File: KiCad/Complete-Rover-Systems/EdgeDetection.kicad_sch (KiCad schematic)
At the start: 9 parts, among them U1 ITR8307-F43, U10 74LS151, U3 ITR8307-F43, U4 ITR8307-F43, U5 ITR8307-F43, U6 ITR8307-F43, U7 ITR8307-F43, U8 ITR8307-F43, U9 ITR8307-F43

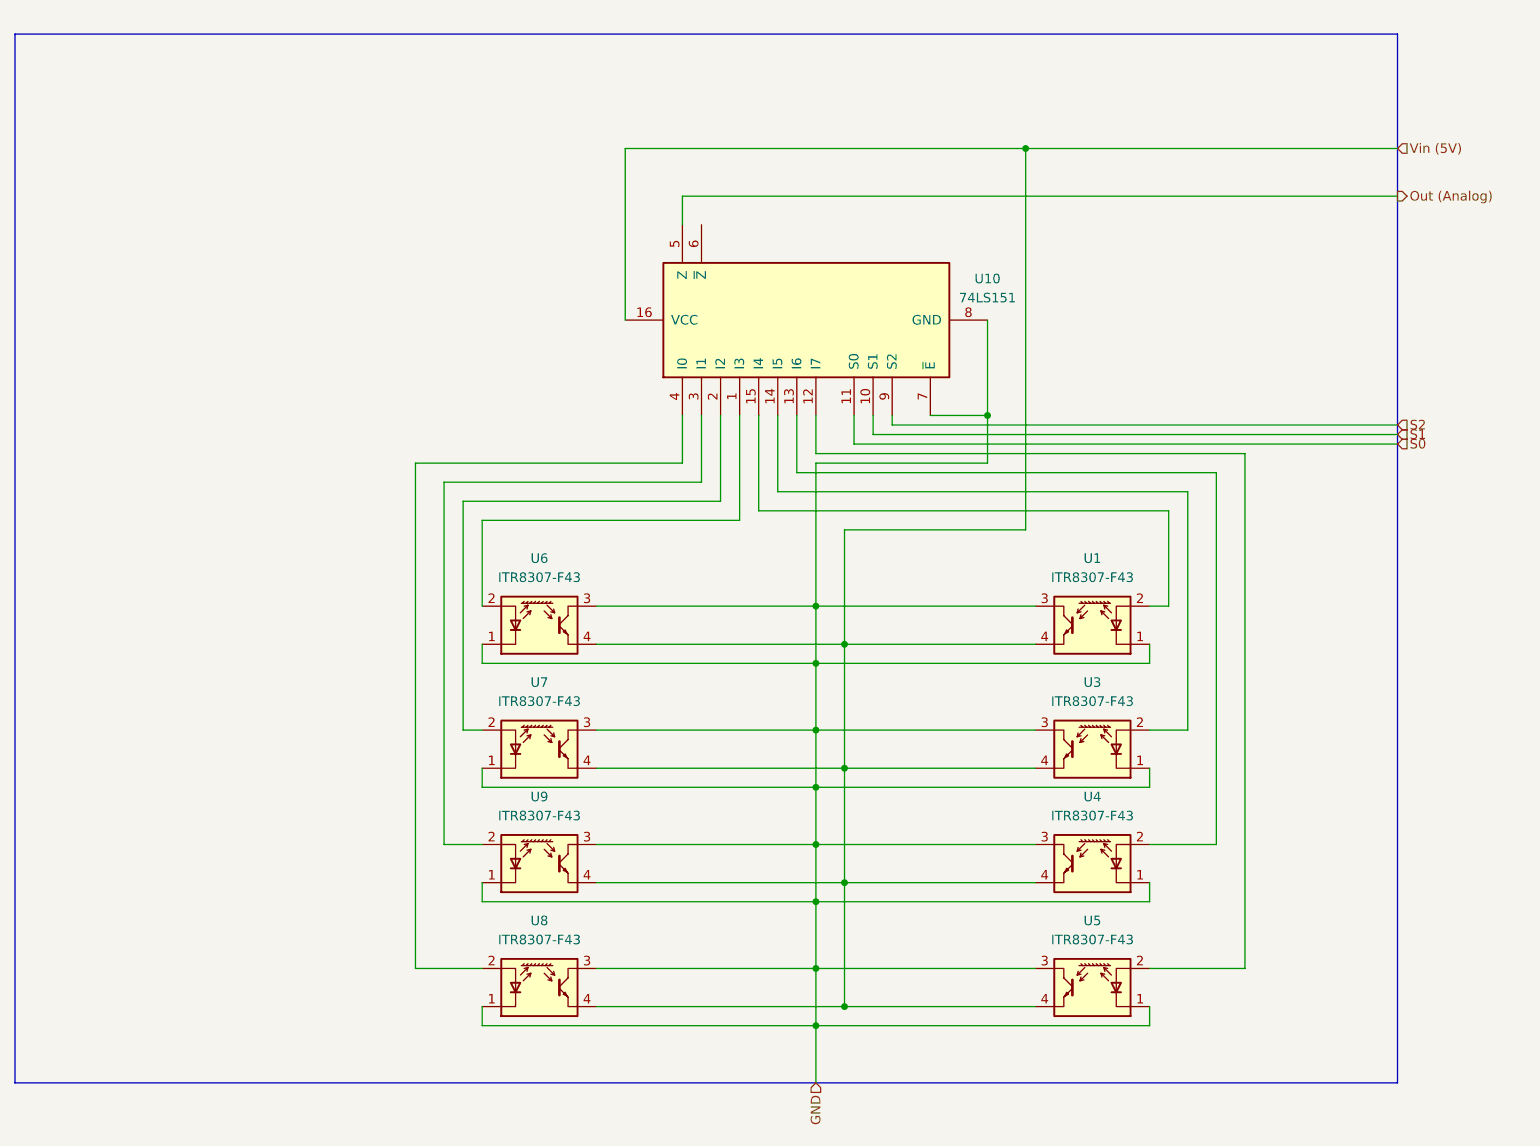
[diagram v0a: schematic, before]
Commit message: edge detection fix
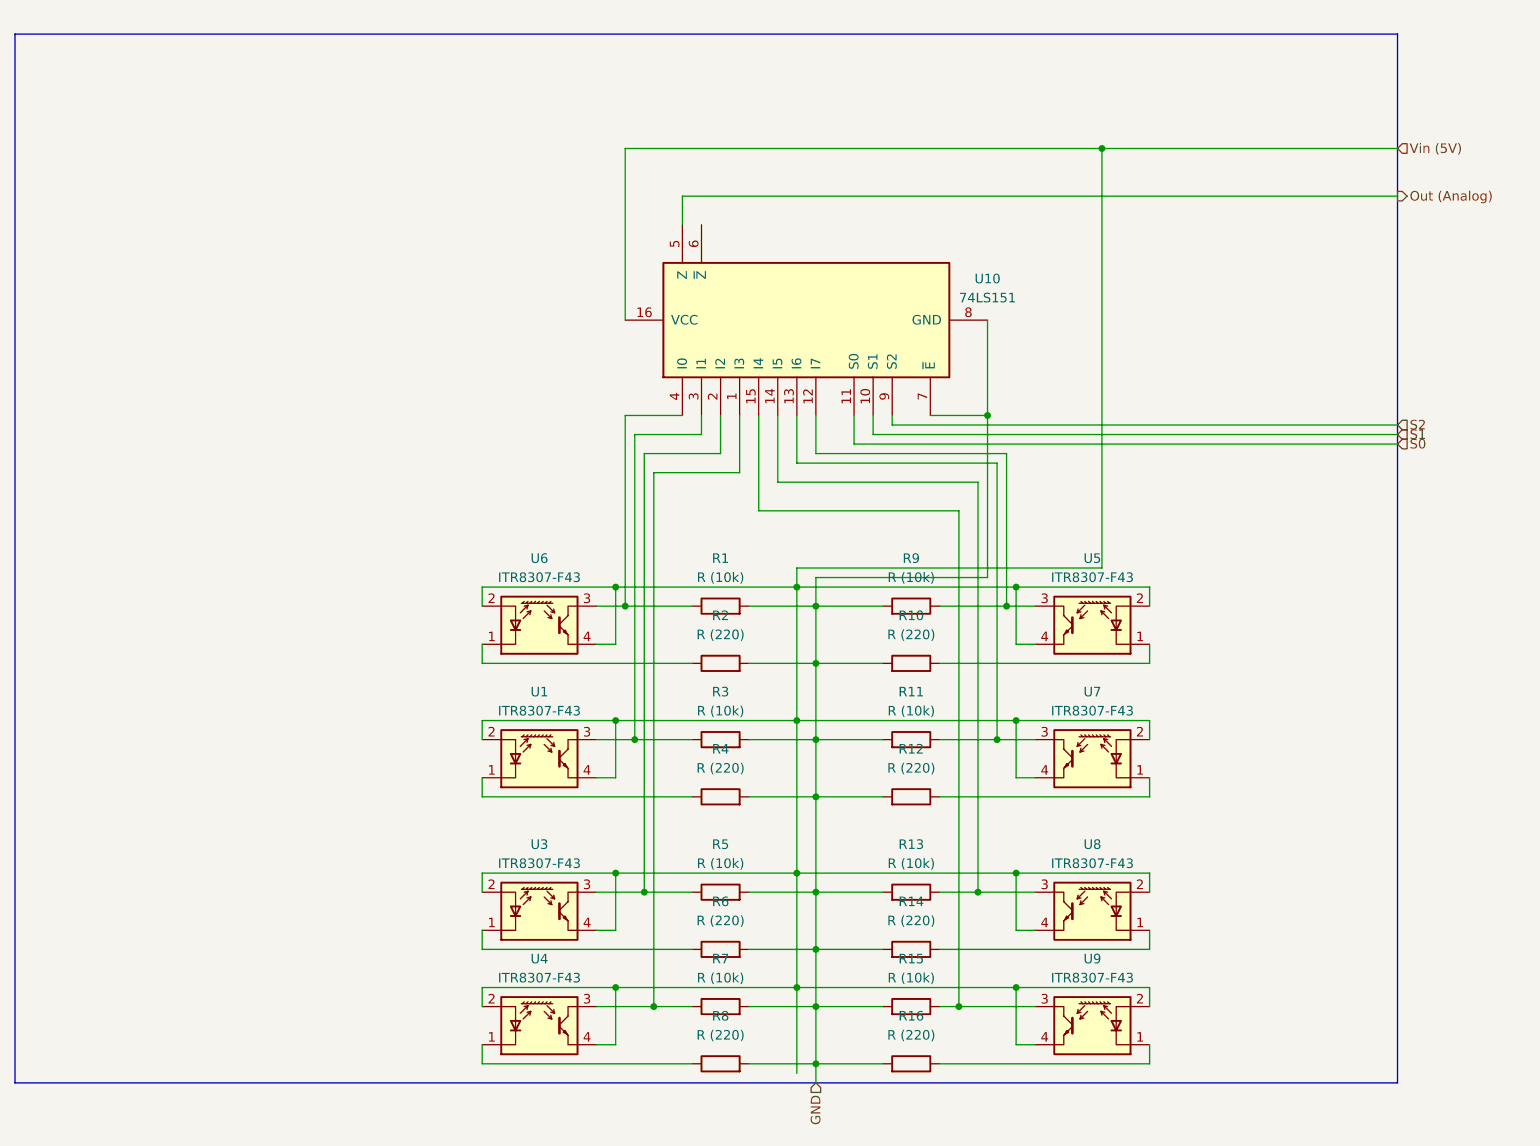
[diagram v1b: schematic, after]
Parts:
- added R1, R11, R13, R15, R3, R5, R7, R9: R (10k), symbol Device:R
- added R10, R12, R14, R16, R2, R4, R6, R8: R (220), symbol Device:R
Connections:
- net GND: now also R1.2, R10.2, R11.2, R12.2, R13.2, R14.2, R15.2, R16.2, R2.2, R3.2, R4.2, R5.2, R6.2, R7.2, R8.2, R9.2; no longer U1.1 (K), U1.3 (C), U3.1 (K), U3.3 (C), U4.1 (K), U4.3 (C), U5.1 (K), U5.3 (C), U6.1 (K), U6.3 (C), U7.1 (K), U7.3 (C), U8.1 (K), U8.3 (C), U9.1 (K), U9.3 (C)
- net Vin (5V): now also U1.2 (A), U3.2 (A), U4.2 (A), U5.2 (A), U6.2 (A), U7.2 (A), U8.2 (A), U9.2 (A)
- net at U10.14 (I5): now also U8.3 (C), R13.1; no longer U3.2 (A)
- net at U10.13 (I6): now also U7.3 (C), R11.1; no longer U4.2 (A)
- net at U10.15 (I4): now also U9.3 (C), R15.1; no longer U1.2 (A)
- net at U10.1 (I3): now also U4.3 (C), R7.1; no longer U6.2 (A)
- net at U10.12 (I7): now also U5.3 (C), R9.1; no longer U5.2 (A)
- net at U10.2 (I2): now also U3.3 (C), R5.1; no longer U7.2 (A)
- net at U10.3 (I1): now also U1.3 (C), R3.1; no longer U9.2 (A)
- net at U10.4 (I0): now also U6.3 (C), R1.1; no longer U8.2 (A)
- new net: R2.1, U6.1 (K)
- new net: R4.1, U1.1 (K)
- new net: R8.1, U4.1 (K)
- new net: R10.1, U5.1 (K)
- new net: R6.1, U3.1 (K)
- new net: R14.1, U8.1 (K)
- new net: R16.1, U9.1 (K)
- new net: R12.1, U7.1 (K)

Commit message: updated rover with imu
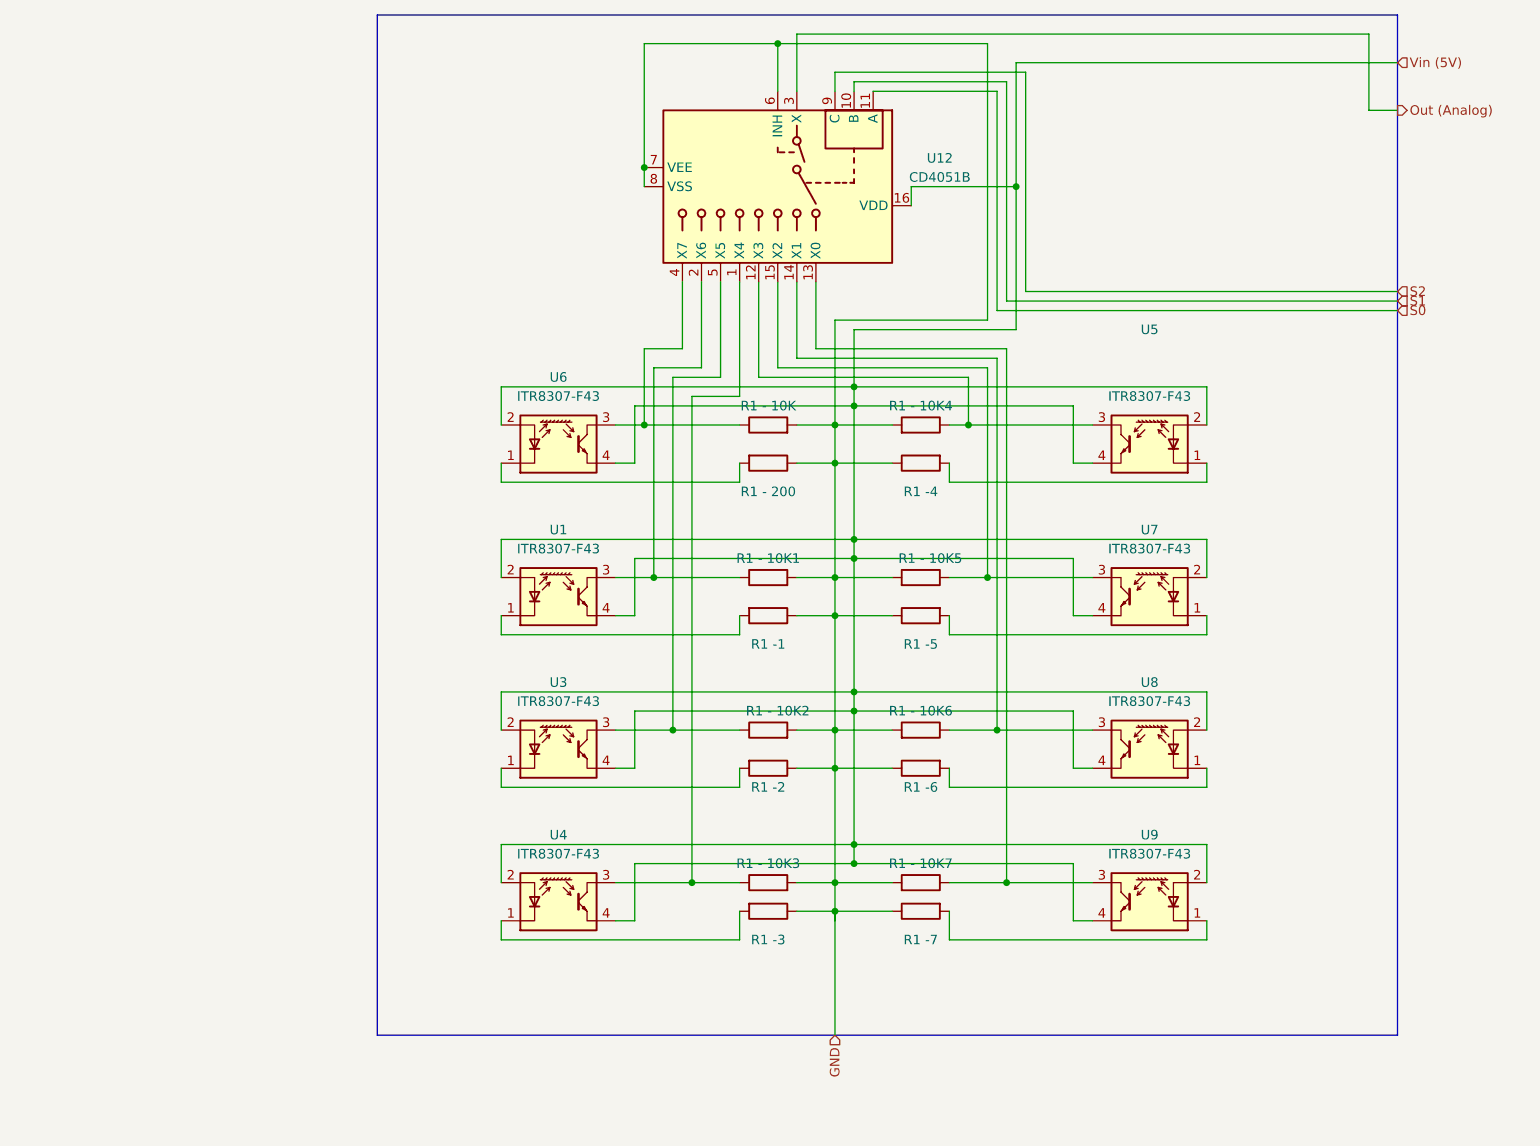
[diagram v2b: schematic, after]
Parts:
- removed R1, R11, R13, R15, R3, R5, R7, R9: R (10k), symbol Device:R
- removed R10, R12, R14, R16, R2, R4, R6, R8: R (220), symbol Device:R
- removed U10: 74LS151, symbol 74xx:74LS151
- added R1 - 10K: R, symbol Device:R
- added R1 - 10K1: R, symbol Device:R
- added R1 - 10K2: R, symbol Device:R
- added R1 - 10K3: R, symbol Device:R
- added R1 - 10K4: R, symbol Device:R
- added R1 - 10K5: R, symbol Device:R
- added R1 - 10K6: R, symbol Device:R
- added R1 - 10K7: R, symbol Device:R
- added R1 - 200: R, symbol Device:R
- added R1 -1: R, symbol Device:R
- added R1 -2: R, symbol Device:R
- added R1 -3: R, symbol Device:R
- added R1 -4: R, symbol Device:R
- added R1 -5: R, symbol Device:R
- added R1 -6: R, symbol Device:R
- added R1 -7: R, symbol Device:R
- added U12: CD4051B, symbol Analog_Switch:CD4051B
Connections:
- net GND: now also R1 - 10K.2, R1 - 10K1.2, R1 - 10K2.2, R1 - 10K3.2, R1 - 10K4.2, R1 - 10K5.2, R1 - 10K6.2, R1 - 10K7.2, R1 - 200.1, R1 -1.1, R1 -2.1, R1 -3.1, R1 -4.1, R1 -5.1, R1 -6.1, R1 -7.1, U12.6 (INH), U12.7 (VEE), U12.8 (VSS)
- net Out (Analog): now also U12.3 (X)
- net S0: now also U12.11 (A)
- net S1: now also U12.10 (B)
- net S2: now also U12.9 (C)
- net Vin (5V): now also U12.16 (VDD)
- net at U3.3 (C): now also R1 - 10K2.1, U12.5 (X5)
- net at U1.3 (C): now also R1 - 10K1.1, U12.2 (X6)
- net at U6.3 (C): now also R1 - 10K.1, U12.4 (X7)
- net at U6.1 (K): now also R1 - 200.2
- net at U4.3 (C): now also R1 - 10K3.1, U12.1 (X4)
- net at U9.3 (C): now also R1 - 10K7.1, U12.13 (X0)
- net at U1.1 (K): now also R1 -1.2
- net at U4.1 (K): now also R1 -3.2
- net at U5.1 (K): now also R1 -4.2
- net at U5.3 (C): now also R1 - 10K4.1, U12.12 (X3)
- net at U3.1 (K): now also R1 -2.2
- net at U8.1 (K): now also R1 -6.2
- net at U8.3 (C): now also R1 - 10K6.1, U12.14 (X1)
- net at U7.3 (C): now also R1 - 10K5.1, U12.15 (X2)
- net at U9.1 (K): now also R1 -7.2
- net at U7.1 (K): now also R1 -5.2
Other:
- moved on the sheet: U6
